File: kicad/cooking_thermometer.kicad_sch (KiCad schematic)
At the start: 59 parts, among them J1 FTDI, J2 STLINK, J3 3V3_Power, J4 Battery, J5 7SEG_CONN, J6 OLED_CONN, J8 THERMO_CONN, J9 USB_C, Q1 BC547, SW1 BOOT0_SW, SW2 NRST_SW, SW3 UI_A_SW, SW4 UI_B_SW, SW5 UI_C_SW, U1 STM32G0B0KETx, U2 MCP1700x-330xxTO, U3 MCP73831-2-OT

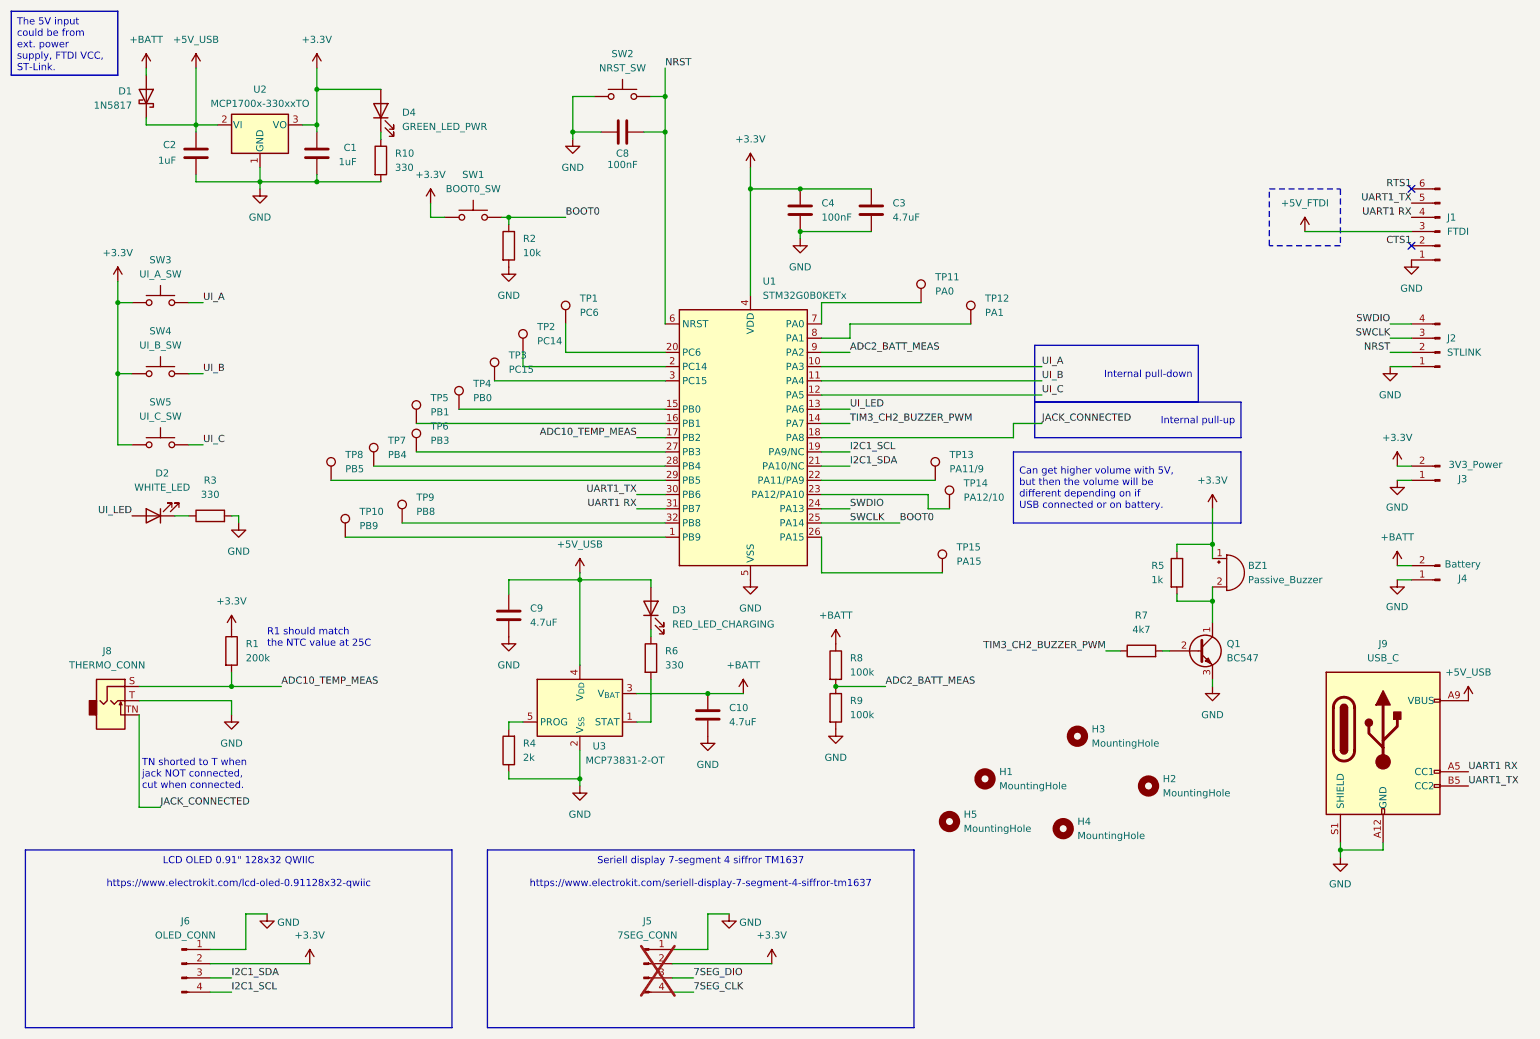
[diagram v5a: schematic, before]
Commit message: Add extra series on pullup NTC. Move stuff around.
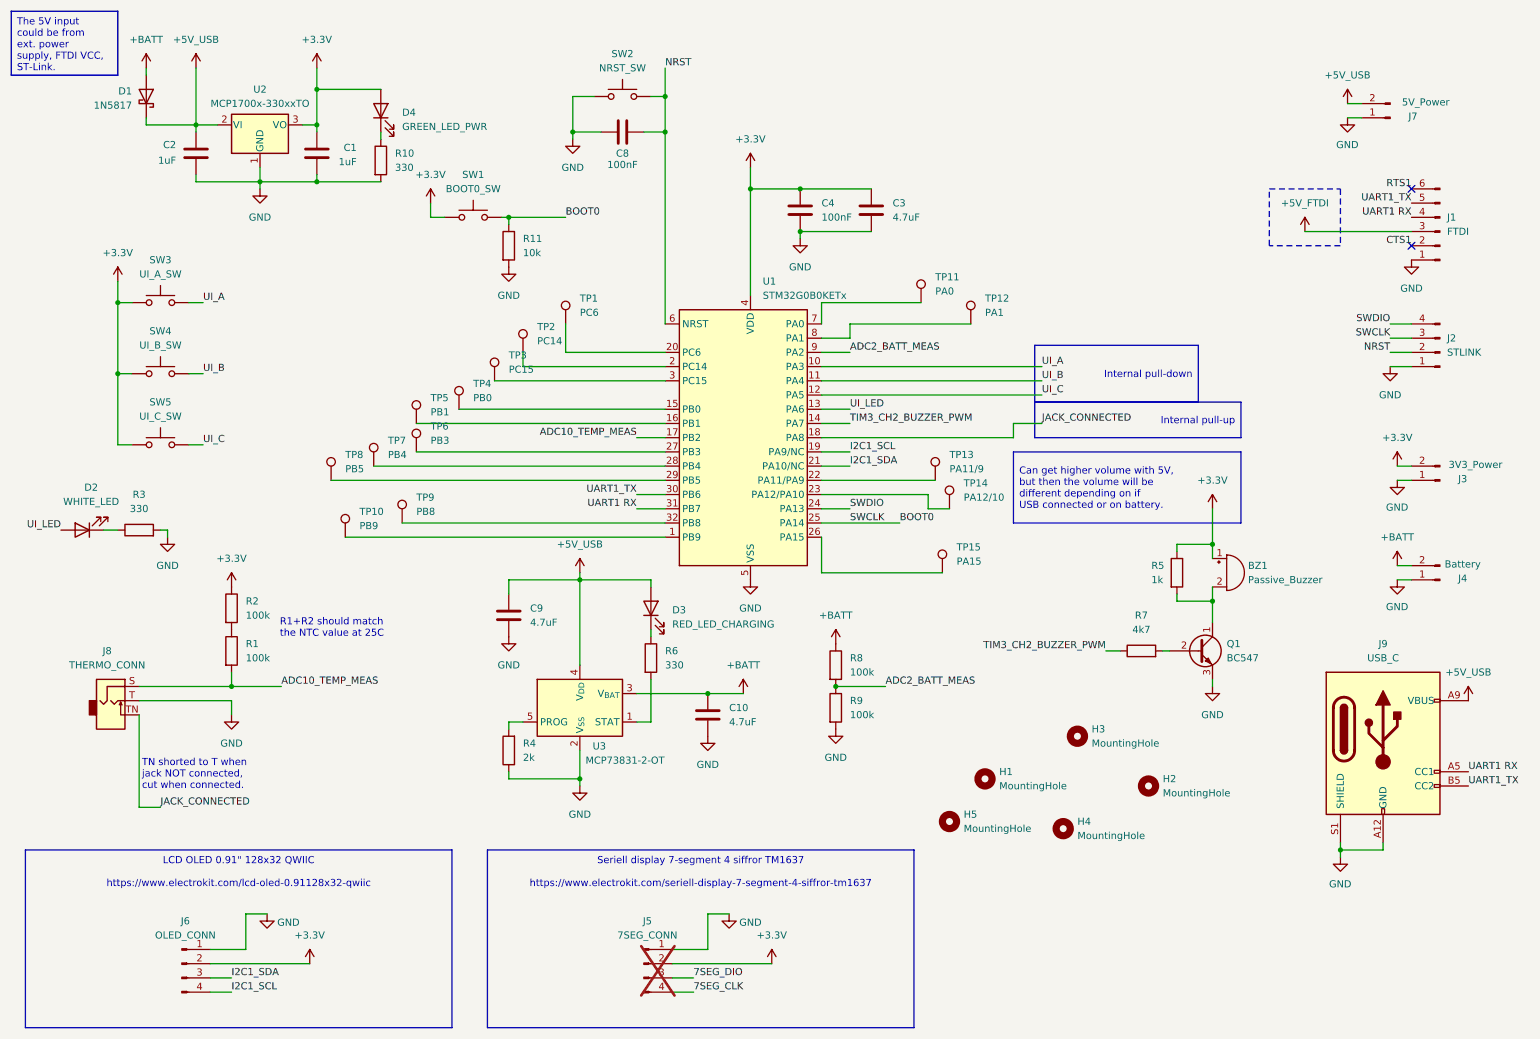
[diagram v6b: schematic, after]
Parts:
- added J7: 5V_Power, Connector_PinHeader_2.54mm:PinHeader_1x02_P2.54mm_Vertical, symbol Connector:Conn_01x02_Pin
- added R2: 100k, Resistor_SMD:R_1206_3216Metric_Pad1.30x1.75mm_HandSolder, symbol Device:R
- R1: value 200k -> 100k
- renumbered R2 to R11
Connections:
- net +3.3V: now also R2.1; no longer R1.1
- net +5V_USB: now also J7.2 (Pin_2)
- net GND: now also J7.1 (Pin_1)
- new net: R1.1, R2.2
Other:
- note added: "R1+R2 should match the NTC value at 25C"
- note removed: "R1 should match the NTC value at 25C"
- moved on the sheet: D2, R3

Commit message: Update schematic and board
Add C5 for temperature input stabilization

Rename UI led and buzzer to correctly denote PWM usage
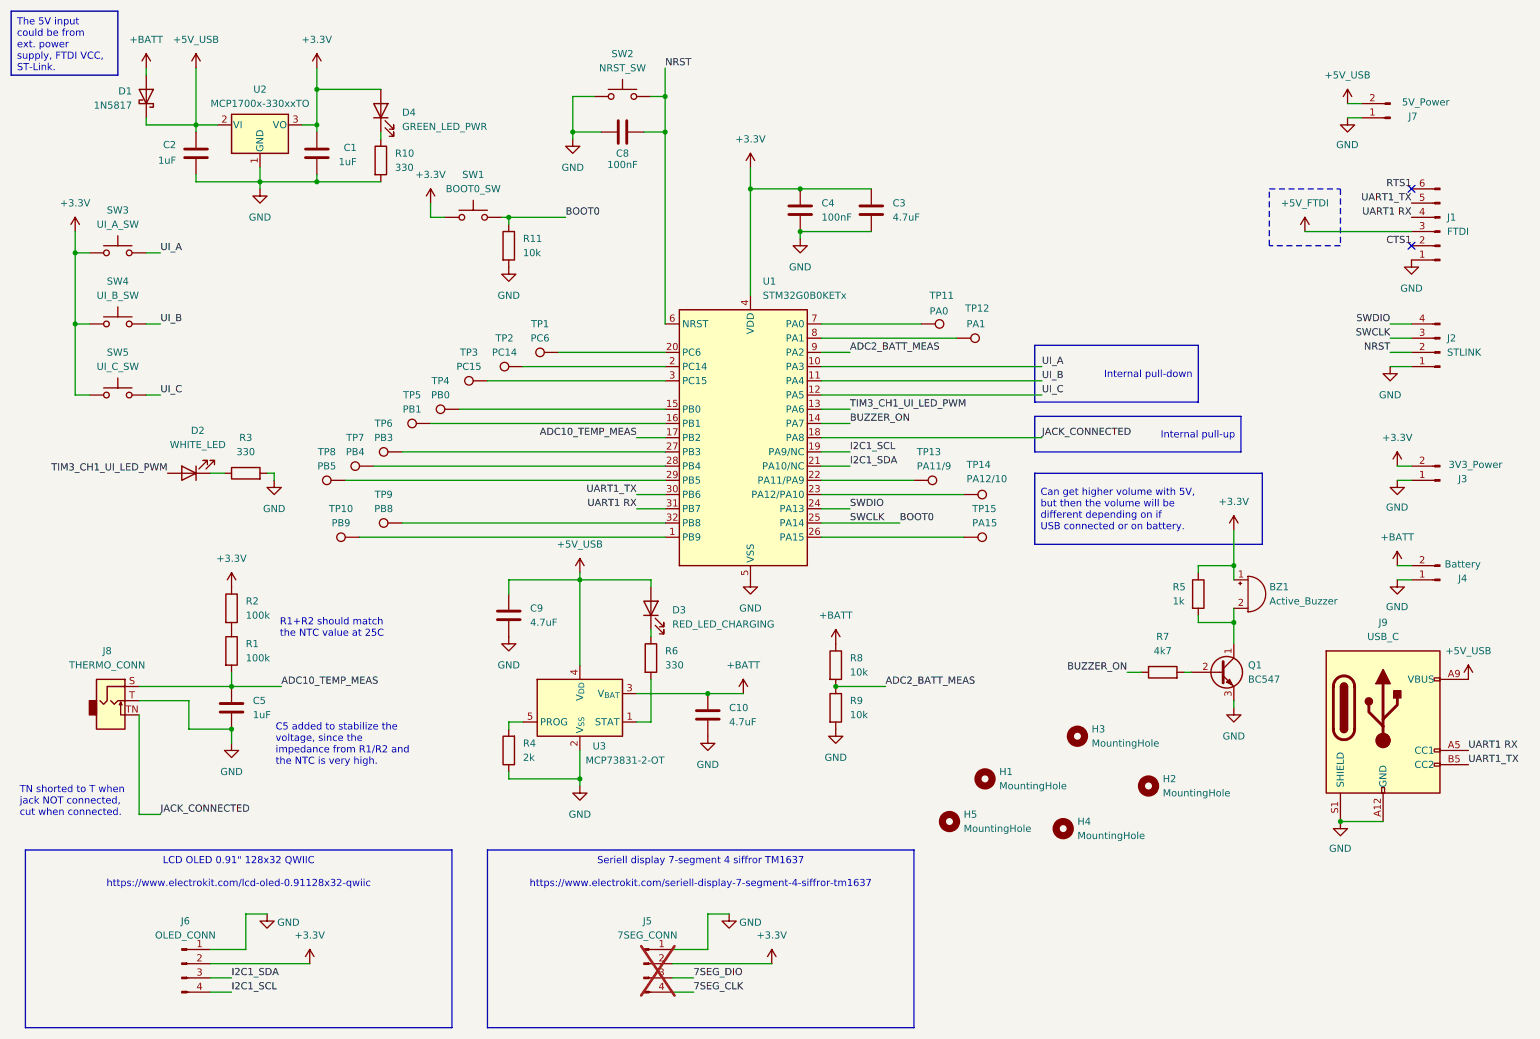
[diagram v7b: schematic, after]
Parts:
- added C5: 1uF, Capacitor_SMD:C_1206_3216Metric_Pad1.33x1.80mm_HandSolder, symbol Device:C
- BZ1: value Passive_Buzzer -> Active_Buzzer
- R8, R9: value 100k -> 10k
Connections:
- net ADC10_TEMP_MEAS: now also C5.1
- net GND: now also C5.2
- net TIM3_CH2_BUZZER_PWM renamed BUZZER_ON
- net UI_LED renamed TIM3_CH1_UI_LED_PWM
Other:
- note added: "C5 added to stabilize the voltage, since the impedance from R1/R2 and the NTC is very high."
- moved on the sheet: BZ1, D2, J9, Q1, R3, R5, R7, SW3, SW4, SW5, TP1, TP10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
